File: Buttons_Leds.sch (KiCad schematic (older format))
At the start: 38 parts, among them P11 CONN_01X06, P12 CONN_01X06, Q2 BC849, Q3 BC849, Q4 BC849, Q5 BC849, SW1 TEC_1, SW2 TEC_1, SW3 TEC_1, SW4 TEC_1

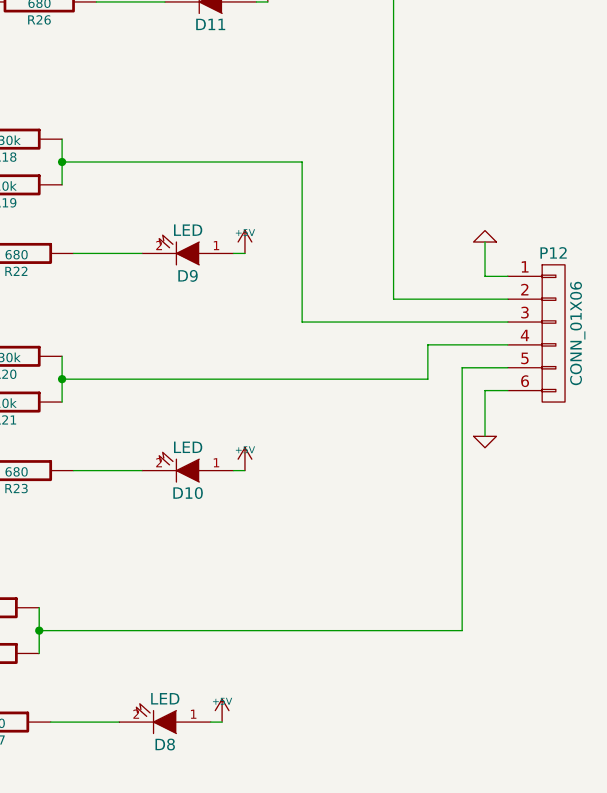
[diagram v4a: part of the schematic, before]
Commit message: Modificaciones en el schematico.Cambio dimension a 10x7 cm.
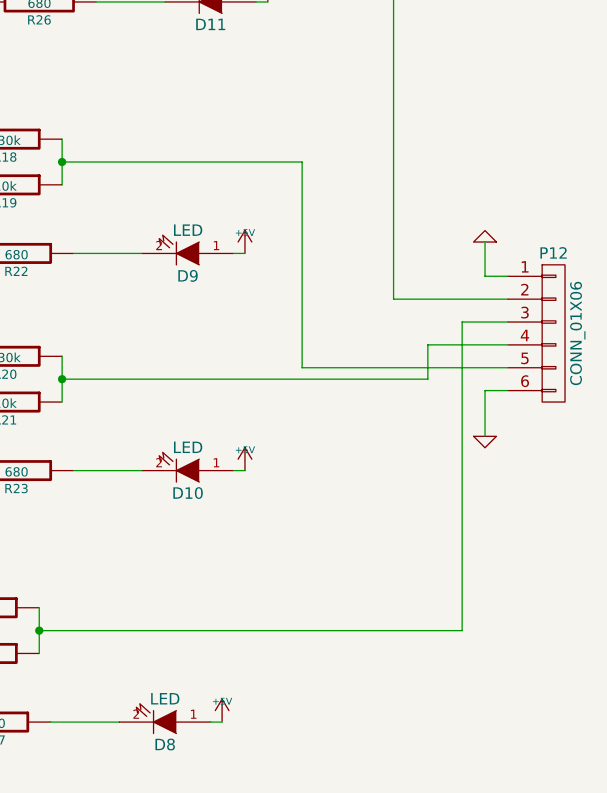
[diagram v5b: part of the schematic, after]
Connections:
- net at R15.1, R16.1: now also P12.3 (P3); no longer P12.5 (P5)
- net at R18.1, R19.1: now also P12.5 (P5); no longer P12.3 (P3)
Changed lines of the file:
@@
 	1150 5050 1500 5050
 Wire Wire Line
-	9050 3800 8850 3800
-Wire Wire Line
-	8850 3800 8850 4950
+	8850 3600 8850 4950
 Wire Wire Line
 	8850 4950 7000 4950
@@
 	8700 3700 9050 3700
 Wire Wire Line
-	9050 3600 8150 3600
-Wire Wire Line
-	8150 3600 8150 2900
+	8150 2900 8150 3800
 Wire Wire Line
 	8550 1800 8550 3500
@@
 	0    1    1    0
 $EndComp
+Wire Wire Line
+	9050 3600 8850 3600
+Wire Wire Line
+	8150 3800 9050 3800
 $EndSCHEMATC

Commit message: Change names schematic.
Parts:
- P11: value CONN_01X06 -> SwPins
- P12: value CONN_01X06 -> PinLeds
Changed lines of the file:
@@
 P 9250 3650
 F 0 "P12" H 9250 4000 50  0000 C CNN
-F 1 "CONN_01X06" V 9350 3650 50  0000 C CNN
+F 1 "PinLeds" V 9350 3650 50  0000 C CNN
 F 2 "Pin_Headers:Pin_Header_Straight_1x06" H 9250 3650 50  0001 C CNN
 F 3 "" H 9250 3650 50  0000 C CNN
@@
 P 650 4050
 F 0 "P11" H 650 4400 50  0000 C CNN
-F 1 "CONN_01X06" V 750 4050 50  0000 C CNN
+F 1 "SwPins" V 750 4050 50  0000 C CNN
 F 2 "Pin_Headers:Pin_Header_Straight_1x06" H 650 4050 50  0001 C CNN
 F 3 "" H 650 4050 50  0000 C CNN

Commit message: Agrego los graficos para el esquematico en 3d.
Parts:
- D10, D11, D8, D9: footprint Diodes_SMD:MELF_Handsoldering -> SMD_Packages:SMD-1206_Pol
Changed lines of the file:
@@
 F 0 "D10" H 7650 4350 50  0000 C CNN
 F 1 "LED" H 7650 4150 50  0000 C CNN
-F 2 "Diodes_SMD:MELF_Handsoldering" H 4750 6550 60  0001 C CNN
+F 2 "SMD_Packages:SMD-1206_Pol" H 4750 6550 60  0001 C CNN
 F 3 "qtlp630c-2.pdf" H 4750 6550 60  0001 C CNN
 F 4 "LED YELLOW WTR CLR 0805 SMD T/R" H 4750 6550 60  0001 C CNN "Descripción"
@@
 F 0 "D8" H 7550 5450 50  0000 C CNN
 F 1 "LED" H 7550 5250 50  0000 C CNN
-F 2 "Diodes_SMD:MELF_Handsoldering" H 4650 7650 60  0001 C CNN
+F 2 "SMD_Packages:SMD-1206_Pol" H 4650 7650 60  0001 C CNN
 F 3 "qtlp630c-2.pdf" H 4650 7650 60  0001 C CNN
 F 4 "LED YELLOW WTR CLR 0805 SMD T/R" H 4650 7650 60  0001 C CNN "Descripción"
@@
 F 0 "D11" H 7750 2300 50  0000 C CNN
 F 1 "LED" H 7750 2100 50  0000 C CNN
-F 2 "Diodes_SMD:MELF_Handsoldering" H 4850 4500 60  0001 C CNN
+F 2 "SMD_Packages:SMD-1206_Pol" H 4850 4500 60  0001 C CNN
 F 3 "qtlp630c-2.pdf" H 4850 4500 60  0001 C CNN
 F 4 "LED YELLOW WTR CLR 0805 SMD T/R" H 4850 4500 60  0001 C CNN "Descripción"
@@
 F 0 "D9" H 7650 3400 50  0000 C CNN
 F 1 "LED" H 7650 3200 50  0000 C CNN
-F 2 "Diodes_SMD:MELF_Handsoldering" H 4750 5600 60  0001 C CNN
+F 2 "SMD_Packages:SMD-1206_Pol" H 4750 5600 60  0001 C CNN
 F 3 "qtlp630c-2.pdf" H 4750 5600 60  0001 C CNN
 F 4 "LED YELLOW WTR CLR 0805 SMD T/R" H 4750 5600 60  0001 C CNN "Descripción"
